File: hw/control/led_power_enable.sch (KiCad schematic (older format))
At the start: 6 parts, among them Q903 BC807, Q904 BC817

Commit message: [hw] Re-annotate all components
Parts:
- renumbered Q903 to Q901, Q904 to Q902, R902 to R901, R903 to R902, R905 to R903, R906 to R904
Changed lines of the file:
@@
 AR Path="/614AE8DA/618976F6" Ref="R?"  Part="1"
 AR Path="/614AB031/618976F6" Ref="R?"  Part="1"
-AR Path="/614AB031/618915A5/618976F6" Ref="R905"  Part="1"
-AR Path="/614AE8DA/618915A5/618976F6" Ref="R1210"  Part="1"
-F 0 "R905" V 4293 3900 50  0000 C CNN
+AR Path="/614AB031/618915A5/618976F6" Ref="R903"  Part="1"
+AR Path="/614AE8DA/618915A5/618976F6" Ref="R1203"  Part="1"
+F 0 "R1203" V 4293 3900 50  0000 C CNN
 F 1 "R" V 4384 3900 50  0000 C CNN
 F 2 "Resistor_SMD:R_0805_2012Metric_Pad1.20x1.40mm_HandSolder" V 4430 3900 50  0001 C CNN
@@
 AR Path="/614AE8DA/618976FC" Ref="Q?"  Part="1"
 AR Path="/614AB031/618976FC" Ref="Q?"  Part="1"
-AR Path="/614AB031/618915A5/618976FC" Ref="Q904"  Part="1"
+AR Path="/614AB031/618915A5/618976FC" Ref="Q902"  Part="1"
 AR Path="/614AE8DA/618915A5/618976FC" Ref="Q1202"  Part="1"
-F 0 "Q904" H 5191 3946 50  0000 L CNN
+F 0 "Q1202" H 5191 3946 50  0000 L CNN
 F 1 "BC817" H 5191 3855 50  0000 L CNN
 F 2 "Package_TO_SOT_SMD:SOT-23_Handsoldering" H 5200 4000 50  0001 C CNN
@@
 AR Path="/614AE8DA/61897703" Ref="Q?"  Part="1"
 AR Path="/614AB031/61897703" Ref="Q?"  Part="1"
-AR Path="/614AB031/618915A5/61897703" Ref="Q903"  Part="1"
+AR Path="/614AB031/618915A5/61897703" Ref="Q901"  Part="1"
 AR Path="/614AE8DA/618915A5/61897703" Ref="Q1201"  Part="1"
-F 0 "Q903" H 5791 3004 50  0000 L CNN
+F 0 "Q1201" H 5791 3004 50  0000 L CNN
 F 1 "BC807" H 5791 3095 50  0000 L CNN
 F 2 "Package_TO_SOT_SMD:SOT-23_Handsoldering" H 5800 3150 50  0001 C CNN
@@
 AR Path="/614AE8DA/61897709" Ref="R?"  Part="1"
 AR Path="/614AB031/61897709" Ref="R?"  Part="1"
-AR Path="/614AB031/618915A5/61897709" Ref="R903"  Part="1"
-AR Path="/614AE8DA/618915A5/61897709" Ref="R1208"  Part="1"
-F 0 "R903" H 5170 3396 50  0000 L CNN
+AR Path="/614AB031/618915A5/61897709" Ref="R902"  Part="1"
+AR Path="/614AE8DA/618915A5/61897709" Ref="R1202"  Part="1"
+F 0 "R1202" H 5170 3396 50  0000 L CNN
 F 1 "R" H 5170 3305 50  0000 L CNN
 F 2 "Resistor_SMD:R_0805_2012Metric_Pad1.20x1.40mm_HandSolder" V 5030 3350 50  0001 C CNN
@@
 AR Path="/614AE8DA/6189770F" Ref="R?"  Part="1"
 AR Path="/614AB031/6189770F" Ref="R?"  Part="1"
-AR Path="/614AB031/618915A5/6189770F" Ref="R902"  Part="1"
-AR Path="/614AE8DA/618915A5/6189770F" Ref="R1207"  Part="1"
-F 0 "R902" H 5170 2796 50  0000 L CNN
+AR Path="/614AB031/618915A5/6189770F" Ref="R901"  Part="1"
+AR Path="/614AE8DA/618915A5/6189770F" Ref="R1201"  Part="1"
+F 0 "R1201" H 5170 2796 50  0000 L CNN
 F 1 "R" H 5170 2705 50  0000 L CNN
 F 2 "Resistor_SMD:R_0805_2012Metric_Pad1.20x1.40mm_HandSolder" V 5030 2750 50  0001 C CNN
@@
 AR Path="/614AE8DA/61897715" Ref="#PWR?"  Part="1"
 AR Path="/614AB031/61897715" Ref="#PWR?"  Part="1"
-AR Path="/614AB031/618915A5/61897715" Ref="#PWR0105"  Part="1"
-AR Path="/614AE8DA/618915A5/61897715" Ref="#PWR0108"  Part="1"
-F 0 "#PWR0108" H 5100 4150 50  0001 C CNN
+AR Path="/614AB031/618915A5/61897715" Ref="#PWR0902"  Part="1"
+AR Path="/614AE8DA/618915A5/61897715" Ref="#PWR01202"  Part="1"
+F 0 "#PWR01202" H 5100 4150 50  0001 C CNN
 F 1 "GND" H 5105 4227 50  0000 C CNN
 F 2 "" H 5100 4400 50  0001 C CNN
@@
 AR Path="/614AE8DA/6189771D" Ref="#PWR?"  Part="1"
 AR Path="/614AB031/6189771D" Ref="#PWR?"  Part="1"
-AR Path="/614AB031/618915A5/6189771D" Ref="#PWR0106"  Part="1"
-AR Path="/614AE8DA/618915A5/6189771D" Ref="#PWR0109"  Part="1"
-F 0 "#PWR0109" H 5700 2150 50  0001 C CNN
+AR Path="/614AB031/618915A5/6189771D" Ref="#PWR0901"  Part="1"
+AR Path="/614AE8DA/618915A5/6189771D" Ref="#PWR01201"  Part="1"
+F 0 "#PWR01201" H 5700 2150 50  0001 C CNN
 F 1 "+5V" H 5715 2473 50  0000 C CNN
 F 2 "" H 5700 2300 50  0001 C CNN
@@
 AR Path="/614AE8DA/61897733" Ref="R?"  Part="1"
 AR Path="/614AB031/61897733" Ref="R?"  Part="1"
-AR Path="/614AB031/618915A5/61897733" Ref="R906"  Part="1"
-AR Path="/614AE8DA/618915A5/61897733" Ref="R1211"  Part="1"
-F 0 "R906" V 4643 5050 50  0000 C CNN
+AR Path="/614AB031/618915A5/61897733" Ref="R904"  Part="1"
+AR Path="/614AE8DA/618915A5/61897733" Ref="R1204"  Part="1"
+F 0 "R1204" V 4643 5050 50  0000 C CNN
 F 1 "R" V 4734 5050 50  0000 C CNN
 F 2 "Resistor_SMD:R_0805_2012Metric_Pad1.20x1.40mm_HandSolder" V 4780 5050 50  0001 C CNN

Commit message: [hw] Minor updates in control layout
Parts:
- added R905: 10K, Resistor_SMD:R_0805_2012Metric_Pad1.20x1.40mm_HandSolder, symbol Device:R
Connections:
- net EN: now also R905.1
- net GND: now also R905.2
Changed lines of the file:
@@
 $Descr A4 11693 8268
 encoding utf-8
-Sheet 9 15
+Sheet 12 15
 Title ""
 Date ""
@@
 EN
 Wire Wire Line
-	5700 3400 6500 3400
+	5700 3400 5900 3400
+$Comp
+L power:GND #PWR?
+U 1 1 61886956
+P 5900 3900
+AR Path="/614AB031/61886956" Ref="#PWR?"  Part="1"
+AR Path="/614AE8DA/61886956" Ref="#PWR?"  Part="1"
+AR Path="/614AB031/618915A5/61886956" Ref="#PWR0903"  Part="1"
+AR Path="/614AE8DA/618915A5/61886956" Ref="#PWR01203"  Part="1"
+F 0 "#PWR01203" H 5900 3650 50  0001 C CNN
+F 1 "GND" H 5905 3727 50  0000 C CNN
+F 2 "" H 5900 3900 50  0001 C CNN
+F 3 "" H 5900 3900 50  0001 C CNN
+	1    5900 3900
+	1    0    0    -1
+$EndComp
+Wire Wire Line
+	5900 3900 5900 3800
+$Comp
+L Device:R R?
+U 1 1 6188695E
+P 5900 3650
+AR Path="/614AE8DA/6188695E" Ref="R?"  Part="1"
+AR Path="/614AB031/6188695E" Ref="R?"  Part="1"
+AR Path="/614AB031/618915A5/6188695E" Ref="R905"  Part="1"
+AR Path="/614AE8DA/618915A5/6188695E" Ref="R1205"  Part="1"
+F 0 "R1205" H 5970 3696 50  0000 L CNN
+F 1 "10K" H 5970 3605 50  0000 L CNN
+F 2 "Resistor_SMD:R_0805_2012Metric_Pad1.20x1.40mm_HandSolder" V 5830 3650 50  0001 C CNN
+F 3 "~" H 5900 3650 50  0001 C CNN
+	1    5900 3650
+	1    0    0    -1
+$EndComp
+Wire Wire Line
+	5900 3500 5900 3400
+Connection ~ 5900 3400
+Wire Wire Line
+	5900 3400 6500 3400
 $EndSCHEMATC

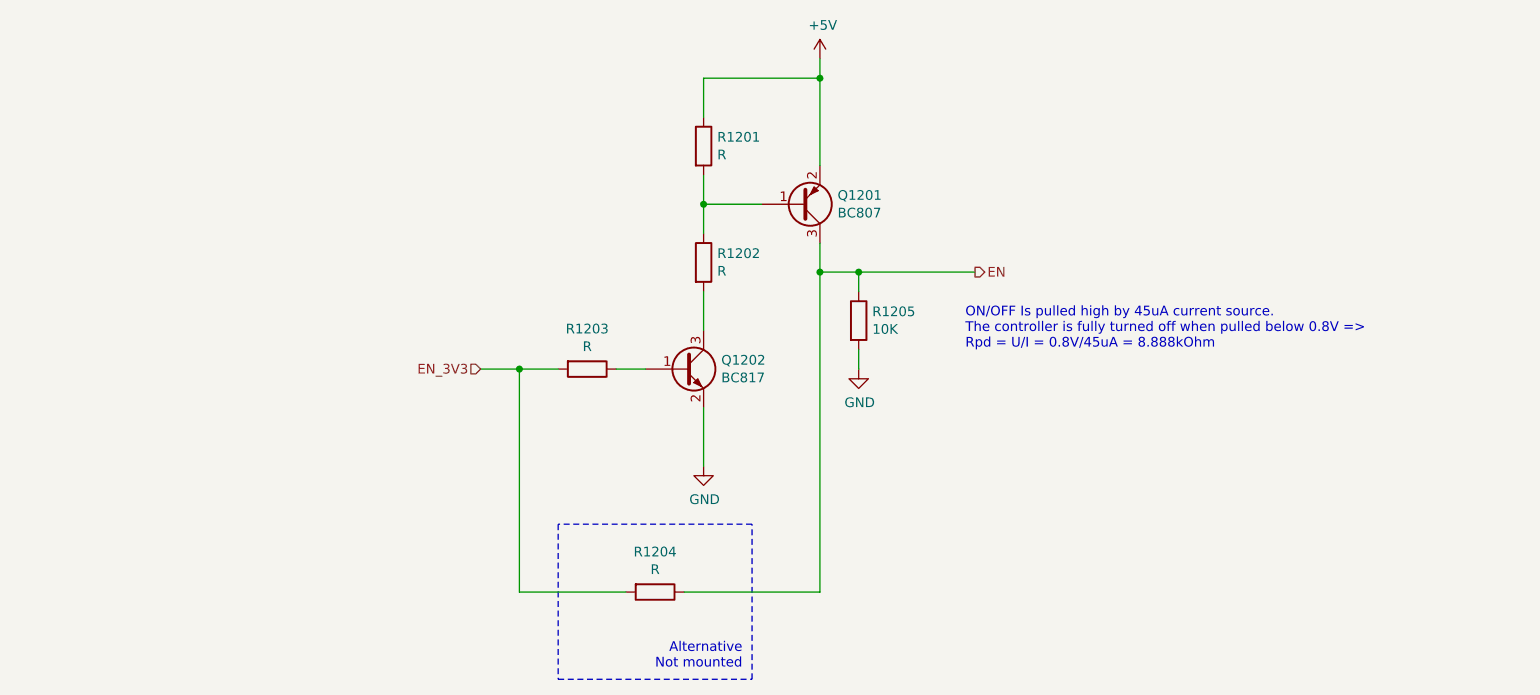
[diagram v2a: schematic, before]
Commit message: [hw] Add missing resistor values
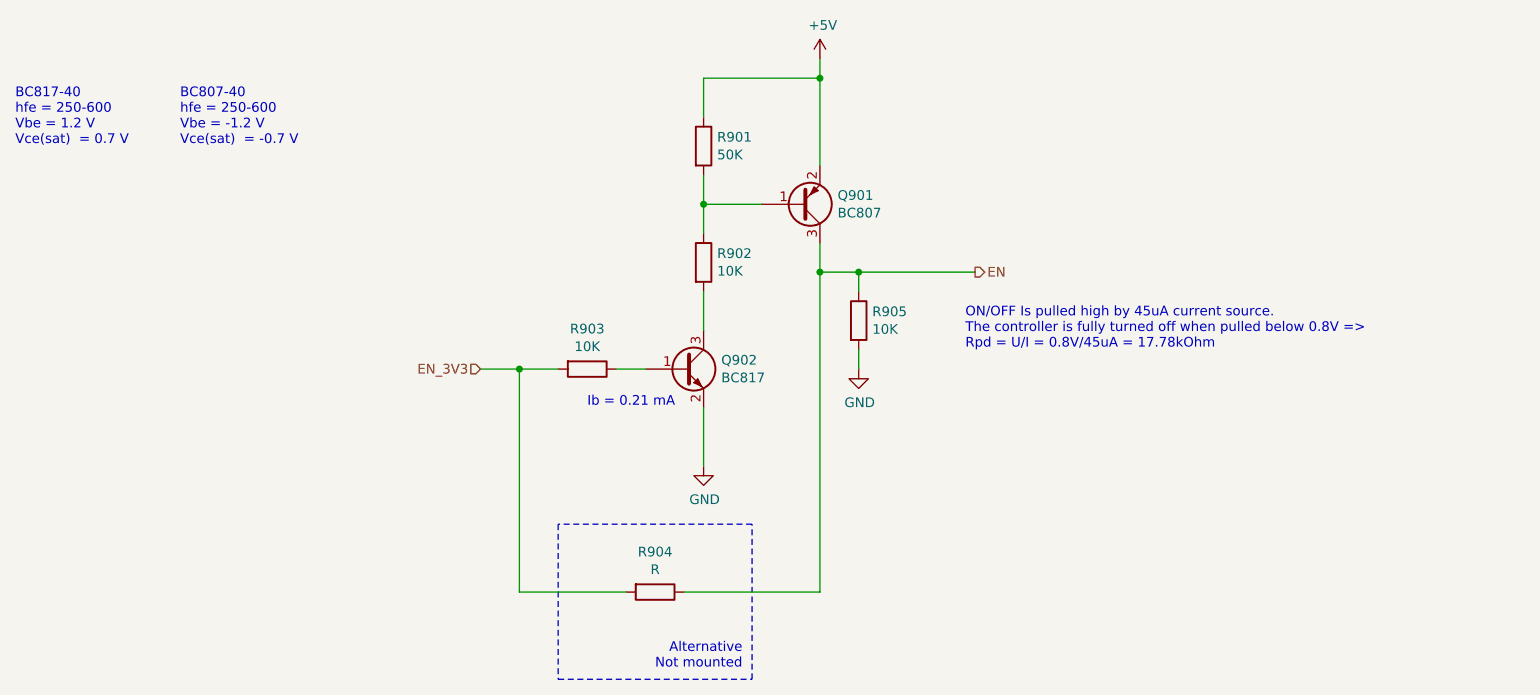
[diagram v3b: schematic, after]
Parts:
- R901: value R -> 50K
- R902, R903: value R -> 10K
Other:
- note added: "BC807-40\nhfe = 250-600\nVbe = -1.2 V\nVce(sat) = -0.7 V"
- note added: "BC817-40\nhfe = 250-600\nVbe = 1.2 V\nVce(sat) = 0.7 V"
- note added: "Ib = 0.21 mA"
- note added: "ON/OFF Is pulled high by 45uA current source.\nThe controller is fully turned off when pulled below 0.8V =>\nRpd = U/I = 0.8V/45uA = 17.78kOhm"
- note removed: "ON/OFF Is pulled high by 45uA current source.\nThe controller is fully turned off when pulled below 0.8V =>\nRpd = U/I = 0.8V/45uA = 8.888kOhm"
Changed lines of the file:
@@
 $Descr A4 11693 8268
 encoding utf-8
-Sheet 12 15
+Sheet 9 15
 Title ""
 Date ""
@@
 AR Path="/614AB031/618915A5/618976F6" Ref="R903"  Part="1"
 AR Path="/614AE8DA/618915A5/618976F6" Ref="R1203"  Part="1"
-F 0 "R1203" V 4293 3900 50  0000 C CNN
-F 1 "R" V 4384 3900 50  0000 C CNN
+F 0 "R903" V 4293 3900 50  0000 C CNN
+F 1 "10K" V 4384 3900 50  0000 C CNN
 F 2 "Resistor_SMD:R_0805_2012Metric_Pad1.20x1.40mm_HandSolder" V 4430 3900 50  0001 C CNN
 F 3 "~" H 4500 3900 50  0001 C CNN
@@
 AR Path="/614AB031/618915A5/618976FC" Ref="Q902"  Part="1"
 AR Path="/614AE8DA/618915A5/618976FC" Ref="Q1202"  Part="1"
-F 0 "Q1202" H 5191 3946 50  0000 L CNN
+F 0 "Q902" H 5191 3946 50  0000 L CNN
 F 1 "BC817" H 5191 3855 50  0000 L CNN
 F 2 "Package_TO_SOT_SMD:SOT-23_Handsoldering" H 5200 4000 50  0001 C CNN
@@
 AR Path="/614AB031/618915A5/61897703" Ref="Q901"  Part="1"
 AR Path="/614AE8DA/618915A5/61897703" Ref="Q1201"  Part="1"
-F 0 "Q1201" H 5791 3004 50  0000 L CNN
+F 0 "Q901" H 5791 3004 50  0000 L CNN
 F 1 "BC807" H 5791 3095 50  0000 L CNN
 F 2 "Package_TO_SOT_SMD:SOT-23_Handsoldering" H 5800 3150 50  0001 C CNN
@@
 AR Path="/614AB031/618915A5/61897709" Ref="R902"  Part="1"
 AR Path="/614AE8DA/618915A5/61897709" Ref="R1202"  Part="1"
-F 0 "R1202" H 5170 3396 50  0000 L CNN
-F 1 "R" H 5170 3305 50  0000 L CNN
+F 0 "R902" H 5170 3396 50  0000 L CNN
+F 1 "10K" H 5170 3305 50  0000 L CNN
 F 2 "Resistor_SMD:R_0805_2012Metric_Pad1.20x1.40mm_HandSolder" V 5030 3350 50  0001 C CNN
 F 3 "~" H 5100 3350 50  0001 C CNN
@@
 AR Path="/614AB031/618915A5/6189770F" Ref="R901"  Part="1"
 AR Path="/614AE8DA/618915A5/6189770F" Ref="R1201"  Part="1"
-F 0 "R1201" H 5170 2796 50  0000 L CNN
-F 1 "R" H 5170 2705 50  0000 L CNN
+F 0 "R901" H 5170 2796 50  0000 L CNN
+F 1 "50K" H 5170 2705 50  0000 L CNN
 F 2 "Resistor_SMD:R_0805_2012Metric_Pad1.20x1.40mm_HandSolder" V 5030 2750 50  0001 C CNN
 F 3 "~" H 5100 2750 50  0001 C CNN
@@
 AR Path="/614AB031/618915A5/61897715" Ref="#PWR0902"  Part="1"
 AR Path="/614AE8DA/618915A5/61897715" Ref="#PWR01202"  Part="1"
-F 0 "#PWR01202" H 5100 4150 50  0001 C CNN
+F 0 "#PWR0902" H 5100 4150 50  0001 C CNN
 F 1 "GND" H 5105 4227 50  0000 C CNN
 F 2 "" H 5100 4400 50  0001 C CNN
@@
 AR Path="/614AB031/618915A5/6189771D" Ref="#PWR0901"  Part="1"
 AR Path="/614AE8DA/618915A5/6189771D" Ref="#PWR01201"  Part="1"
-F 0 "#PWR01201" H 5700 2150 50  0001 C CNN
+F 0 "#PWR0901" H 5700 2150 50  0001 C CNN
 F 1 "+5V" H 5715 2473 50  0000 C CNN
 F 2 "" H 5700 2300 50  0001 C CNN
@@
 AR Path="/614AB031/618915A5/61897733" Ref="R904"  Part="1"
 AR Path="/614AE8DA/618915A5/61897733" Ref="R1204"  Part="1"
-F 0 "R1204" V 4643 5050 50  0000 C CNN
+F 0 "R904" V 4643 5050 50  0000 C CNN
 F 1 "R" V 4734 5050 50  0000 C CNN
 F 2 "Resistor_SMD:R_0805_2012Metric_Pad1.20x1.40mm_HandSolder" V 4780 5050 50  0001 C CNN
@@
 	5350 4700 4350 4700
 Text Notes 6450 3800 0    50   ~ 0
-ON/OFF Is pulled high by 45uA current source.\nThe controller is fully turned off when pulled below 0.8V =>\nRpd = U/I = 0.8V/45uA = 8.888kOhm
+ON/OFF Is pulled high by 45uA current source.\nThe controller is fully turned off when pulled below 0.8V =>\nRpd = U/I = 0.8V/45uA = 17.78kOhm
 Wire Wire Line
 	5100 4100 5100 4400
@@
 AR Path="/614AB031/618915A5/61886956" Ref="#PWR0903"  Part="1"
 AR Path="/614AE8DA/618915A5/61886956" Ref="#PWR01203"  Part="1"
-F 0 "#PWR01203" H 5900 3650 50  0001 C CNN
+F 0 "#PWR0903" H 5900 3650 50  0001 C CNN
 F 1 "GND" H 5905 3727 50  0000 C CNN
 F 2 "" H 5900 3900 50  0001 C CNN
@@
 AR Path="/614AB031/618915A5/6188695E" Ref="R905"  Part="1"
 AR Path="/614AE8DA/618915A5/6188695E" Ref="R1205"  Part="1"
-F 0 "R1205" H 5970 3696 50  0000 L CNN
+F 0 "R905" H 5970 3696 50  0000 L CNN
 F 1 "10K" H 5970 3605 50  0000 L CNN
 F 2 "Resistor_SMD:R_0805_2012Metric_Pad1.20x1.40mm_HandSolder" V 5830 3650 50  0001 C CNN
@@
 Wire Wire Line
 	5900 3400 6500 3400
+Text Notes 1550 2750 0    50   ~ 0
+BC817-40\nhfe = 250-600\nVbe = 1.2 V\nVce(sat)  = 0.7 V
+Text Notes 2400 2750 0    50   ~ 0
+BC807-40\nhfe = 250-600\nVbe = -1.2 V\nVce(sat)  = -0.7 V
+Text Notes 4500 4100 0    50   ~ 0
+Ib = 0.21 mA
 $EndSCHEMATC
